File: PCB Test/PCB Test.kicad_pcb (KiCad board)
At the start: 2 copper layers, 0 parts

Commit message: Started on the PCB Layout, added ENEL270 programming pin, fixed motor voltages
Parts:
- added BT1: Battery_Cell, Battery:BatteryHolder_Keystone_2462_2xAA, F.Cu at (119.7, 88.5)
- added BT2: Battery_Cell, Battery:BatteryHolder_Keystone_2462_2xAA, F.Cu at (119.7, 123.7)
- added C1: 10u, Capacitor_THT:C_Radial_D6.3mm_H5.0mm_P2.50mm, F.Cu at (140.5, 135.0)
- added C2: 10u, Capacitor_THT:C_Radial_D6.3mm_H5.0mm_P2.50mm, F.Cu at (144.3, 45.8)
- added C3: 22n, Capacitor_SMD:C_0805_2012Metric_Pad1.18x1.45mm_HandSolder, F.Cu at (151.0, 102.7)
- added C4: 1u, Capacitor_THT:C_Radial_D6.3mm_H5.0mm_P2.50mm, F.Cu at (128.0, 124.0)
- added C5: 10n, Capacitor_SMD:C_0805_2012Metric_Pad1.18x1.45mm_HandSolder, F.Cu at (113.2, 138.0)
- added C6: 10n, Capacitor_SMD:C_0805_2012Metric_Pad1.18x1.45mm_HandSolder, F.Cu at (113.2, 141.0)
- added C7: 1u, Capacitor_THT:C_Radial_D6.3mm_H5.0mm_P2.50mm, F.Cu at (128.0, 115.5)
- added C8: 100n, Capacitor_SMD:C_0805_2012Metric_Pad1.18x1.45mm_HandSolder, F.Cu at (151.0, 97.1)
- added C9: 100n, Capacitor_SMD:C_0805_2012Metric_Pad1.18x1.45mm_HandSolder, F.Cu at (141.0, 104.7)
- added D1: D_Schottky, Diode_SMD:D_SMA, F.Cu at (89.6, 153.3)
- added D10: LED, LED_THT:LED_D5.0mm, F.Cu at (151.2, 38.1)
- added D11: LED, LED_THT:LED_D5.0mm, F.Cu at (128.0, 134.5)
- added D2: D_Schottky, Diode_SMD:D_SMA, F.Cu at (89.6, 157.8)
- added D8: LED, LED_THT:LED_D5.0mm, F.Cu at (187.5, 59.8)
- added D9: LED, LED_THT:LED_D5.0mm, F.Cu at (187.5, 66.5)
- added J1: Motor Terminal 2, TerminalBlock:TerminalBlock_MaiXu_MX126-5.0-02P_1x02_P5.00mm, F.Cu at (147.5, 128.5)
- added J2: Conn_02x05_Odd_Even, Connector_PinSocket_1.00mm:PinSocket_2x05_P1.00mm_Vertical_SMD, F.Cu at (160.1, 90.2)
- added J5: Motor Terminal 1, TerminalBlock:TerminalBlock_MaiXu_MX126-5.0-02P_1x02_P5.00mm, F.Cu at (148.5, 68.5)
- added J6: Conn_02x03_Odd_Even, Connector_PinSocket_1.00mm:PinSocket_2x03_P1.00mm_Vertical_SMD, F.Cu at (160.1, 96.7)
- added Q2: NMOS, Package_TO_SOT_SMD:SOT-23, F.Cu at (206.9, 33.8)
- added Q3: NMOS, Package_TO_SOT_SMD:SOT-23, F.Cu at (211.7, 33.8)
- added R1: 10k, Resistor_SMD:R_0805_2012Metric_Pad1.20x1.40mm_HandSolder, F.Cu at (154.0, 99.7)
- added R10: 47, Resistor_SMD:R_0805_2012Metric_Pad1.20x1.40mm_HandSolder, F.Cu at (200.0, 46.0)
- added R11: 10k, Resistor_SMD:R_0805_2012Metric_Pad1.20x1.40mm_HandSolder, F.Cu at (202.9, 46.0)
- added R12: 47, Resistor_SMD:R_0805_2012Metric_Pad1.20x1.40mm_HandSolder, F.Cu at (188.2, 41.3)
- added R13: 10k, Resistor_SMD:R_0805_2012Metric_Pad1.20x1.40mm_HandSolder, F.Cu at (191.1, 41.3)
- added R14: 68, Resistor_SMD:R_0805_2012Metric_Pad1.20x1.40mm_HandSolder, F.Cu at (194.1, 41.3)
- added R15: 10k, Resistor_SMD:R_0805_2012Metric_Pad1.20x1.40mm_HandSolder, F.Cu at (197.0, 41.3)
- added R16: 68, Resistor_SMD:R_0805_2012Metric_Pad1.20x1.40mm_HandSolder, F.Cu at (200.0, 41.3)
- added R17: 10k, Resistor_SMD:R_0805_2012Metric_Pad1.20x1.40mm_HandSolder, F.Cu at (202.9, 41.3)
- added R18: 120, Resistor_SMD:R_0805_2012Metric_Pad1.20x1.40mm_HandSolder, F.Cu at (207.0, 51.0)
- added R19: 120, Resistor_SMD:R_0805_2012Metric_Pad1.20x1.40mm_HandSolder, F.Cu at (191.1, 36.5)
- added R20: 150, Resistor_SMD:R_0805_2012Metric_Pad1.20x1.40mm_HandSolder, F.Cu at (138.2, 119.2)
- added R21: 330, Resistor_SMD:R_0805_2012Metric_Pad1.20x1.40mm_HandSolder, F.Cu at (197.0, 36.5)
- added R22: 330, Resistor_SMD:R_0805_2012Metric_Pad1.20x1.40mm_HandSolder, F.Cu at (200.0, 36.5)
- added R7: 150, Resistor_SMD:R_0805_2012Metric_Pad1.20x1.40mm_HandSolder, F.Cu at (209.0, 51.0)
- added R8: 68, Resistor_SMD:R_0805_2012Metric_Pad1.20x1.40mm_HandSolder, F.Cu at (194.1, 46.0)
- added R9: 10k, Resistor_SMD:R_0805_2012Metric_Pad1.20x1.40mm_HandSolder, F.Cu at (197.0, 46.0)
- added SW1: SW_Push, Button_Switch_THT:SW_PUSH_1P1T_6x3.5mm_H4.3_APEM_MJTP1243, F.Cu at (154.2, 102.7)
- added SW2: SW_Push, Button_Switch_THT:SW_PUSH_1P1T_6x3.5mm_H4.3_APEM_MJTP1243, F.Cu at (102.4, 141.0)
- added SW3: SW_Push, Button_Switch_THT:SW_PUSH_1P1T_6x3.5mm_H4.3_APEM_MJTP1243, F.Cu at (102.4, 146.1)
- added U1: ATmega4808-A, Package_QFP:TQFP-32_7x7mm_P0.8mm, F.Cu at (143.3, 97.2)
- added U2: TCRT5000, OptoDevice:Vishay_TCRT5000, F.Cu at (166.5, 45.2)
- added U3: TCRT5000, OptoDevice:Vishay_TCRT5000, F.Cu at (174.1, 45.2)
- added U4: TCRT5000, OptoDevice:Vishay_TCRT5000, F.Cu at (181.6, 45.2)
- added U5: MCP1700x-330xxTO, Package_TO_SOT_THT:TO-92_Inline, F.Cu at (133.5, 120.5)

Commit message: I think finished a rough layout
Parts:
- U2, U3, U4: footprint OptoDevice:Vishay_TCRT5000 -> Connector_Harwin:Harwin_LTek-Male_2x02_P2.00mm_Vertical
- moved D2 95.6 mm to (168.8, 104.2)
- moved D1 87.0 mm to (171.0, 122.8)
- moved R16 83.6 mm to (131.0, 88.5), turned to 0 degrees
- moved SW3 83.3 mm to (152.8, 79.8), turned to 90 degrees
- moved Q3 82.2 mm to (178.2, 108.8), turned to 180 degrees
- moved SW2 82.0 mm to (156.8, 79.8), turned to 90 degrees
- moved R17 77.9 mm to (142.2, 90.2), turned to 0 degrees
- moved R14 73.1 mm to (131.2, 78.8), turned to 0 degrees
- moved C2 70.4 mm to (158.2, 114.8)
- moved C6 69.4 mm to (169.8, 100.8)
- moved R15 67.3 mm to (142.5, 80.8), turned to 0 degrees
- moved R8 67.2 mm to (131.0, 69.2), turned to 0 degrees
- moved J5 64.6 mm to (167.5, 130.2)
- moved R13 64.3 mm to (183.8, 105.2), turned to 0 degrees
- moved R12 64.1 mm to (179.2, 104.8), turned to -90 degrees
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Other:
- board outline added: 163.5 x 125.5 mm

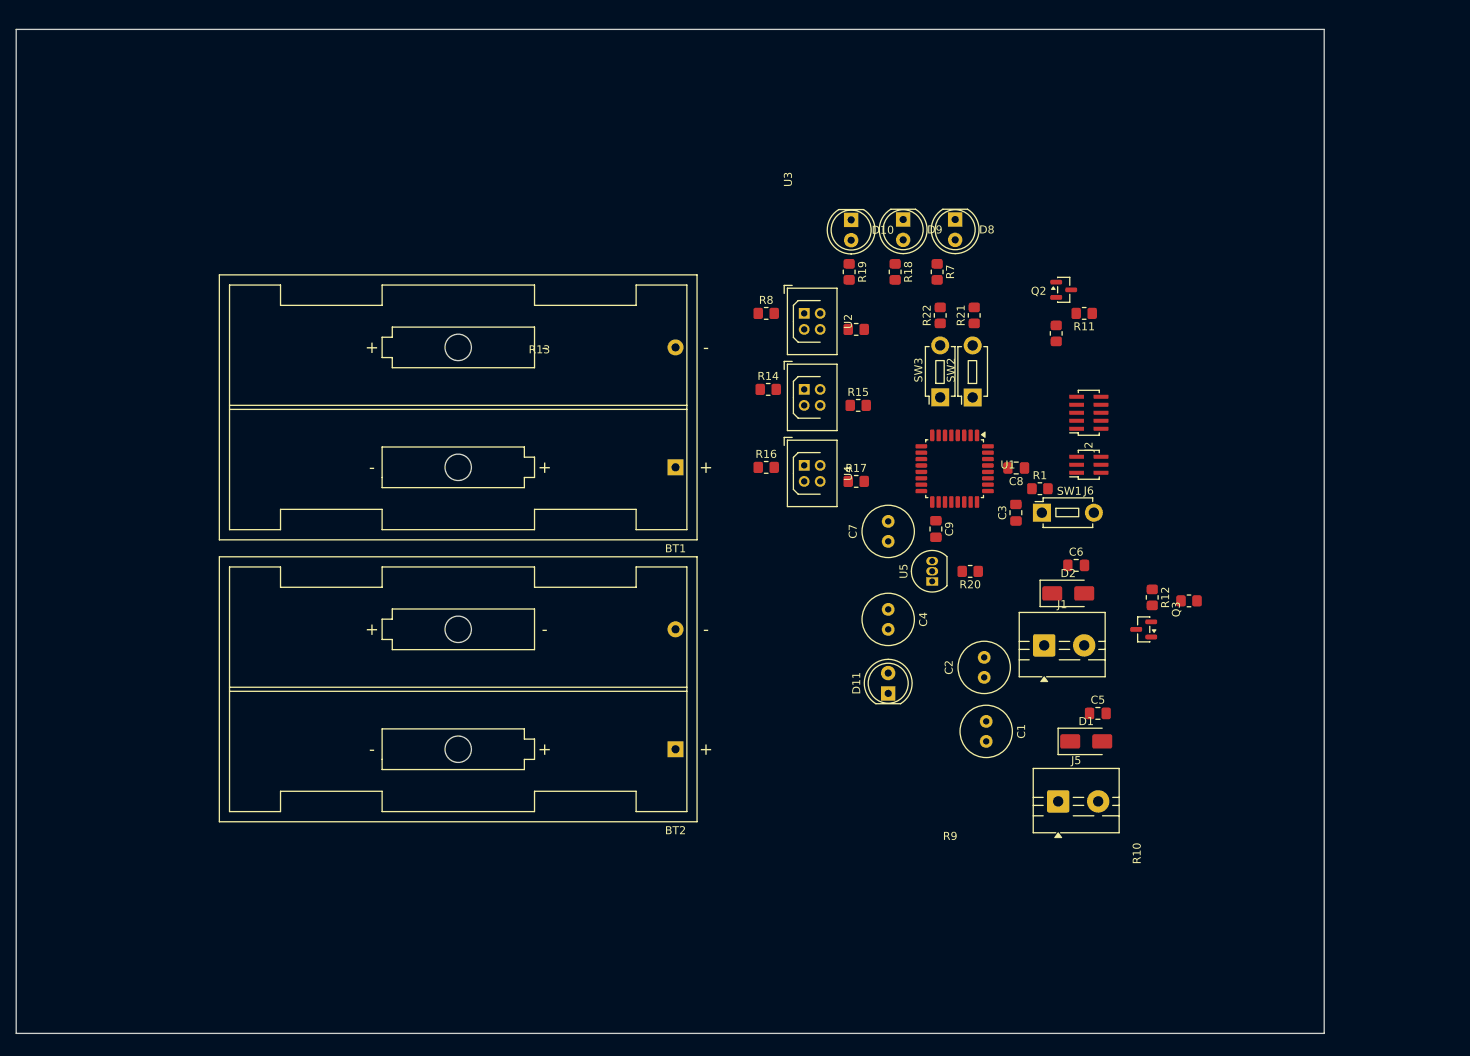
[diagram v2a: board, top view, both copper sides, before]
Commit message: Restructured the board, added a battery connector
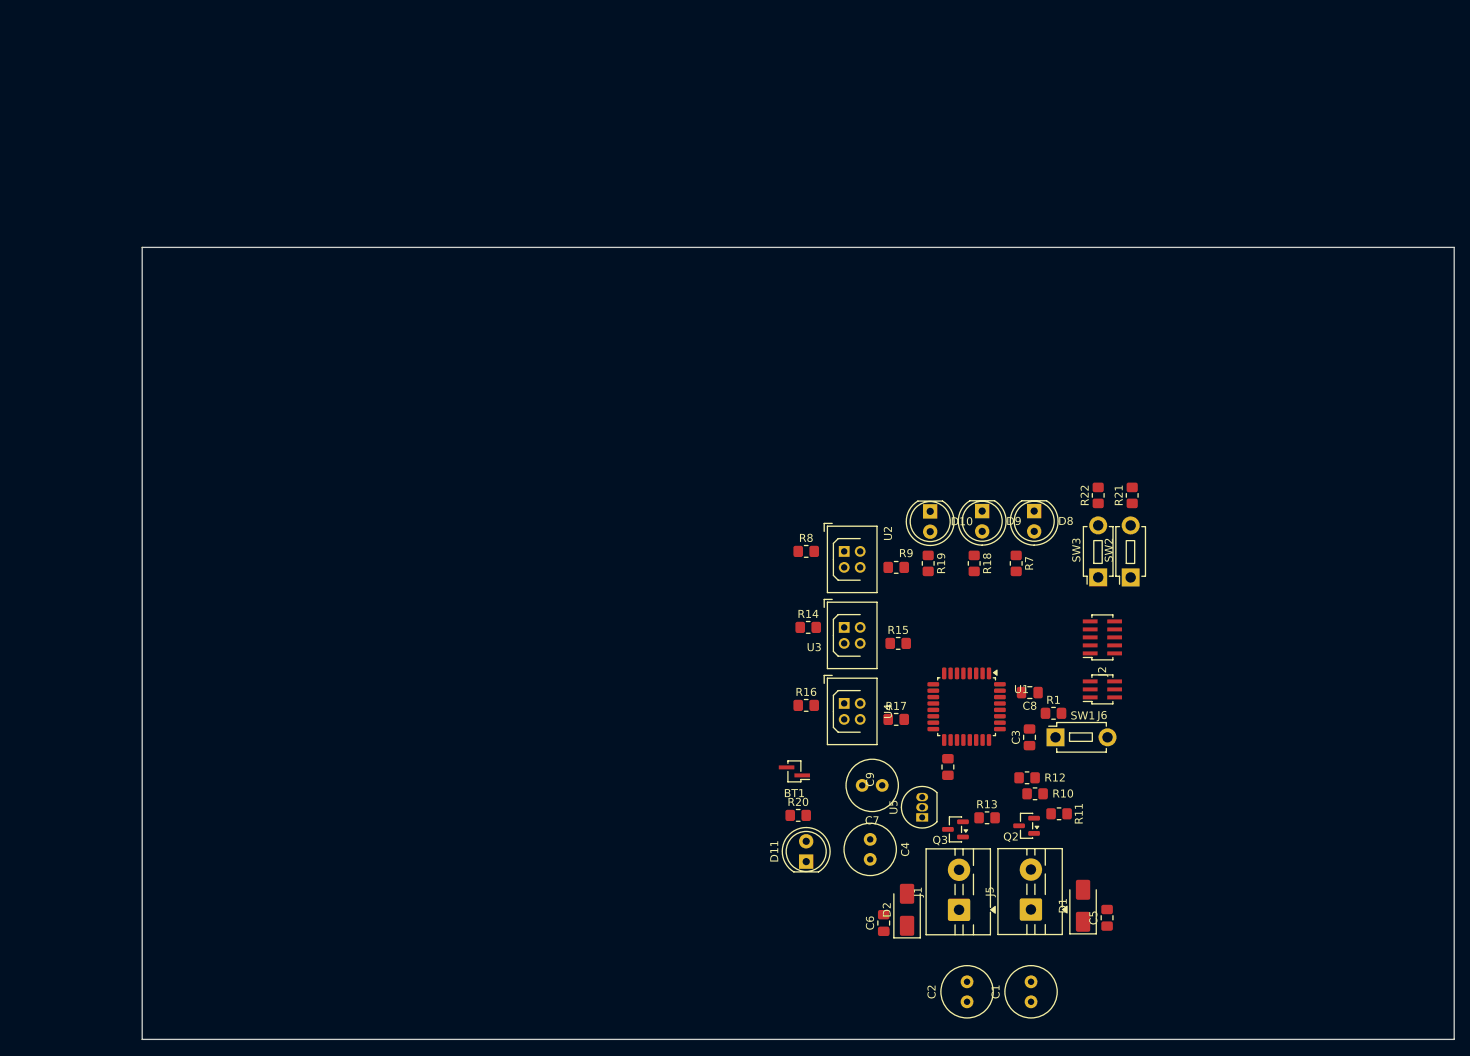
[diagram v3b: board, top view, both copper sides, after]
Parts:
- removed BT2: Battery_Cell, Battery:BatteryHolder_Keystone_2462_2xAA
- BT1: footprint Battery:BatteryHolder_Keystone_2462_2xAA -> Connector_PinSocket_1.00mm:PinSocket_1x02_P1.00mm_Vertical_SMD_Pin1Left
- moved Q2 67.2 mm to (163.5, 133.3), turned to 180 degrees
- moved R11 62.6 mm to (167.6, 131.8), turned to 0 degrees
- moved R10 57.6 mm to (164.6, 129.3), turned to 180 degrees
- moved C6 50.8 mm to (145.7, 145.5), turned to 90 degrees
- moved D2 44.4 mm to (148.6, 143.8), turned to 90 degrees
- moved BT1 40.8 mm to (134.5, 126.5)
- moved C2 40.6 mm to (156.1, 155.3)
- moved D10 37.8 mm to (151.5, 94.0)
- moved R18 37.8 mm to (157.0, 100.5)
- moved R19 37.8 mm to (151.2, 100.5)
- moved R7 37.8 mm to (162.2, 100.5)
- moved D8 37.8 mm to (164.5, 94.0)
- moved D9 37.8 mm to (158.0, 94.0)
- moved R20 37.3 mm to (135.0, 132.0), turned to 0 degrees
- moved R13 37.0 mm to (158.6, 132.3)
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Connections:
- BT1 pad 2: Net-(BT1--) -> GND
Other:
- board size 163.5 x 125.5 mm -> 164 x 99 mm

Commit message: Final layout finished, moving on to motion transmition, need to extract gerber files
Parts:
- removed U2, U3, U4: TCRT5000, Connector_Harwin:Harwin_LTek-Male_2x02_P2.00mm_Vertical
- added H1: MountingHole, MountingHole:MountingHole_2.2mm_M2, F.Cu at (135.6, 91.6)
- added H2: MountingHole, MountingHole:MountingHole_2.2mm_M2, F.Cu at (181.4, 91.4)
- added H3: MountingHole, MountingHole:MountingHole_2.2mm_M2, F.Cu at (181.6, 153.0)
- added H4: MountingHole, MountingHole:MountingHole_2.2mm_M2, F.Cu at (135.6, 153.0)
- added J3: Conn_02x02_Odd_Even, Connector_Harwin:Harwin_LTek-Male_2x02_P2.00mm_Vertical, F.Cu at (140.8, 99.0)
- added J4: Conn_02x02_Odd_Even, Connector_Harwin:Harwin_LTek-Male_2x02_P2.00mm_Vertical, F.Cu at (140.8, 108.5)
- J1: value Motor Terminal 2 -> Conn_02x02_Counter_Clockwise; footprint TerminalBlock:TerminalBlock_MaiXu_MX126-5.0-02P_1x02_P5.00mm -> Connector:NS-Tech_Grove_1x04_P2mm_Vertical
- J2: footprint Connector_PinSocket_1.00mm:PinSocket_2x05_P1.00mm_Vertical_SMD -> Connector_PinHeader_1.00mm:PinHeader_2x05_P1.00mm_Vertical_SMD
- J5: value Motor Terminal 1 -> Conn_02x02_Odd_Even; footprint TerminalBlock:TerminalBlock_MaiXu_MX126-5.0-02P_1x02_P5.00mm -> Connector_Harwin:Harwin_LTek-Male_2x02_P2.00mm_Vertical
- moved J5 34.8 mm to (140.8, 118.0), turned to -90 degrees
- moved J1 8.14 mm to (162.8, 141.0), turned to -90 degrees
- moved C1 2.80 mm to (164.1, 152.5)
- moved C2 2.80 mm to (156.1, 152.5)
- moved C3 2.21 mm to (165.2, 124.0)
- moved BT1 1.73 mm to (135.7, 127.8)
- moved D11 1.73 mm to (137.2, 139.0)
- moved R20 1.73 mm to (136.2, 133.2)
- moved SW1 1.50 mm to (167.8, 123.6)
- moved R22 1.46 mm to (171.1, 91.6), turned to 0 degrees
- moved SW3 1.46 mm to (172.1, 100.8)
- moved SW2 1.46 mm to (176.2, 100.9)
- moved R15 1.30 mm to (146.4, 109.8), turned to 90 degrees
- moved R21 1.22 mm to (175.6, 91.6), turned to 180 degrees
- moved C4 0.94 mm to (143.5, 135.8), turned to 0 degrees
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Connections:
- net USART_RX renamed USART RX
- net USART_TX renamed USART TX
- J1 pad 2: Net-(D2-A) -> Net-(D1-A)
- J5 pad 1: +4.8V -> Net-(J5-Pin_1)
- J5 pad 2: Net-(D1-A) -> +3.3V
- R10 pad 1: Motor 1 -> Motor 2
- R12 pad 1: Motor 2 -> Motor 1
- R16 pad 2: Net-(R16-Pad2) -> Net-(J5-Pin_1)
- R17 pad 1: ADC Sensor 3 -> ADC Sensor 1
- R9 pad 1: ADC Sensor 1 -> ADC Sensor 3
- U1 pad 6: LED_Red -> LED Red
- U1 pad 7: LED Green -> LED Green 1
- U1 pad 8: LED Blue -> LED Green 2
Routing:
- net +3.3V: track 0.00 -> 124.7 mm, vias 0 -> 5
- net +4.8V: track 0.00 -> 102.7 mm
- net GND: track 0.00 -> 87.4 mm, vias 0 -> 27
- net Motor 2: track 0.00 -> 64.6 mm
- net Motor 1: track 0.00 -> 60.3 mm
- net RESET: track 0.00 -> 36.8 mm
- net DTR: track 0.00 -> 34.3 mm
- net Net-(D2-A): track 0.00 -> 29.1 mm
- net Net-(D1-A): track 0.00 -> 27.9 mm
- net Button 1: track 0.00 -> 25.2 mm
- net ADC Sensor 3: track 0.00 -> 23.8 mm
- net Button 2: track 0.00 -> 21.8 mm
- net LED Red: track 0.00 -> 15.8 mm
- net USART TX: track 0.00 -> 15.4 mm
- net USART RX: track 0.00 -> 15.4 mm
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- added copper zone on B.Cu, net GND
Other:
- board size 164 x 99 mm -> 51.6 x 67.2 mm

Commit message: Light polishing
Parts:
- J2: footprint Connector_PinHeader_1.00mm:PinHeader_2x05_P1.00mm_Vertical_SMD -> Connector_PinHeader_1.00mm:PinHeader_2x06_P1.00mm_Vertical
- J6: footprint Connector_PinSocket_1.00mm:PinSocket_2x03_P1.00mm_Vertical_SMD -> Connector_PinSocket_1.27mm:PinSocket_2x03_P1.27mm_Vertical
- moved J2 2.31 mm to (172.5, 107.5)
- moved J6 1.21 mm to (172.4, 117.3)
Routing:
- net +3.3V: track 124.7 -> 120.4 mm
- net RESET: track 36.8 -> 34.8 mm
- net DTR: track 34.3 -> 35.5 mm
- net USART TX: track 15.4 -> 16.6 mm
- net USART RX: track 15.4 -> 16.6 mm
- net UPDI Data: track 12.3 -> 13.2 mm
- net GND: track 87.4 -> 87.6 mm, vias 27 -> 29
